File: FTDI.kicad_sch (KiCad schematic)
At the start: 30 parts, among them J301 USB_B_Micro, U301 93LCxxBxxOT, U302 FT2232HQ, Y301 ABM8-12.000MHZ-20

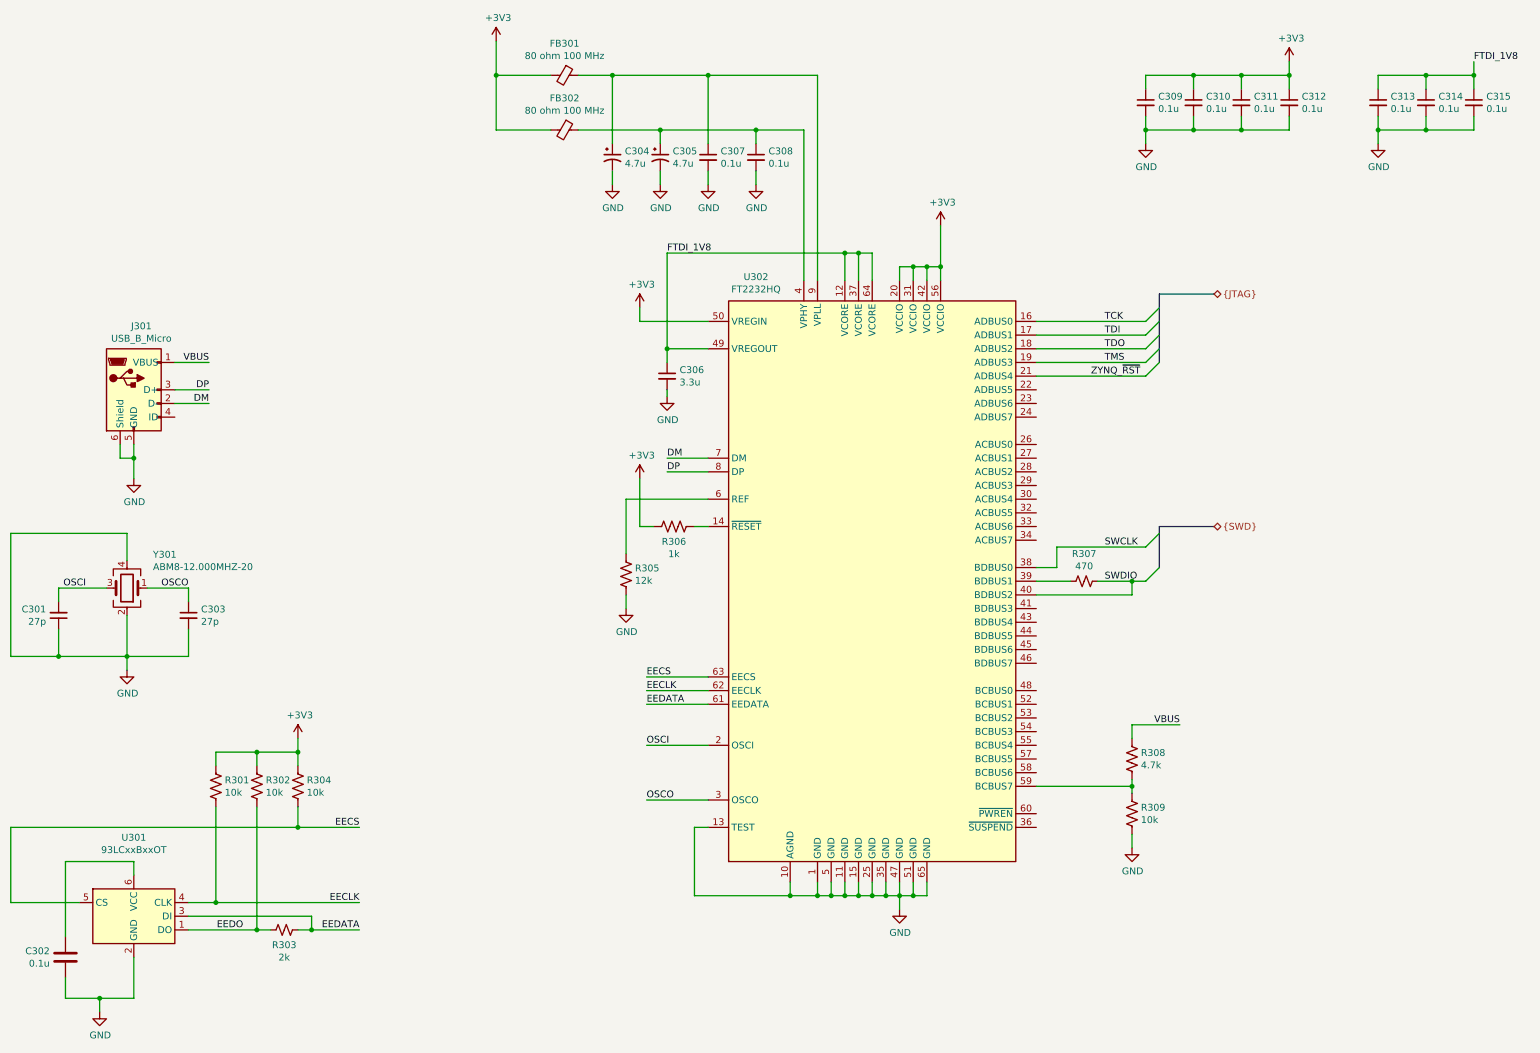
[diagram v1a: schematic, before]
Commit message: Attach ethernet to PL, layout and route
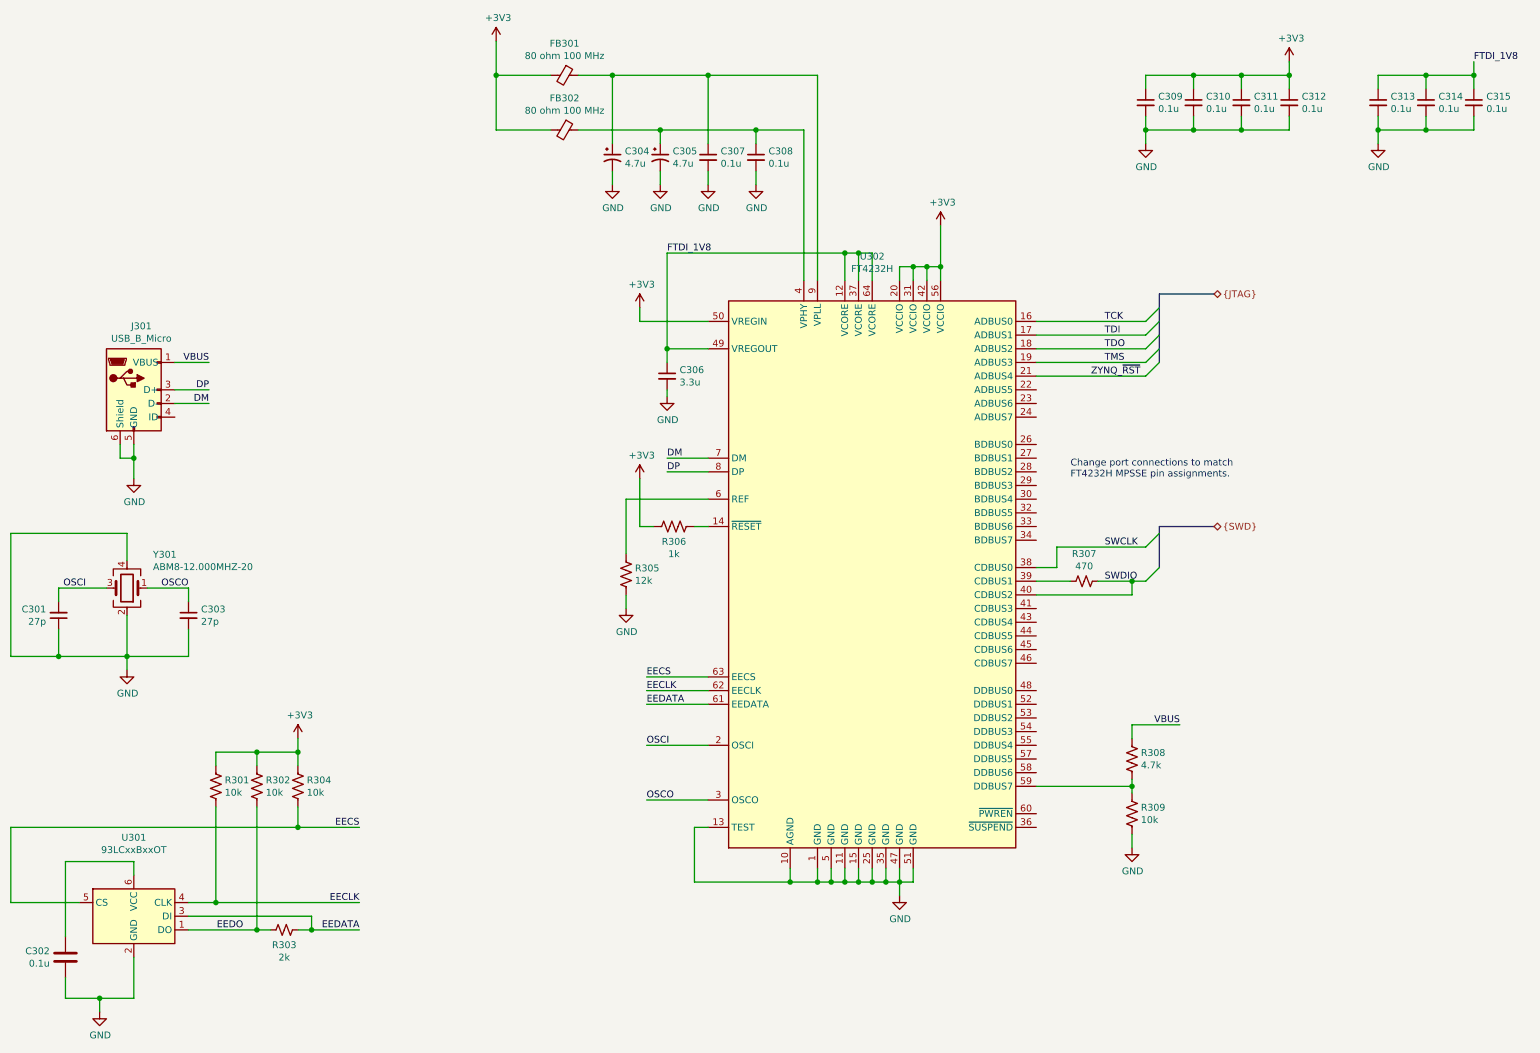
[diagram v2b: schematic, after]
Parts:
- removed U302: FT2232HQ, Package_DFN_QFN:QFN-64-1EP_9x9mm_P0.5mm_EP4.35x4.35mm, symbol Interface_USB:FT2232HQ
- added U302: FT4232H, Package_QFP:LQFP-64_10x10mm_P0.5mm, symbol Interface_USB:FT4232H
- FB301, FB302: footprint Inductor_SMD:L_0603_1608Metric -> Inductor_SMD:L_0402_1005Metric
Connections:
- net +3V3: now also U302.20 (VCCIO), U302.31 (VCCIO), U302.42 (VCCIO), U302.50 (VREGIN), U302.56 (VCCIO)
- net DM: now also U302.7 (DM)
- net DP: now also U302.8 (DP)
- net EECLK: now also U302.62 (EECLK)
- net EECS: now also U302.63 (EECS)
- net EEDATA: now also U302.61 (EEDATA)
- net FTDI_1V8: now also U302.12 (VCORE), U302.37 (VCORE), U302.49 (VREGOUT), U302.64 (VCORE)
- net GND: now also U302.1 (GND), U302.10 (AGND), U302.11 (GND), U302.13 (TEST), U302.15 (GND), U302.25 (GND), U302.35 (GND), U302.47 (GND), U302.5 (GND), U302.51 (GND)
- net OSCI: now also U302.2 (OSCI)
- net OSCO: now also U302.3 (OSCO)
- net SWCLK: now also U302.38 (CDBUS0)
- net SWDIO: now also U302.40 (CDBUS2)
- net TCK: now also U302.16 (ADBUS0)
- net TDI: now also U302.17 (ADBUS1)
- net TDO: now also U302.18 (ADBUS2)
- net TMS: now also U302.19 (ADBUS3)
- net ZYNQ_~RST: now also U302.21 (ADBUS4)
- net at R306.2: now also U302.14 (~RESET)
- net at R308.2, R309.1: now also U302.59 (DDBUS7)
- net at R307.1: now also U302.39 (CDBUS1)
- net at C305.1, C308.1, FB302.1: now also U302.4 (VPHY)
- net at R305.1: now also U302.6 (REF)
- net at C304.1, C307.1, FB301.1: now also U302.9 (VPLL)
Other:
- note added: "Change port connections to match FT4232H MPSSE pin assignments."

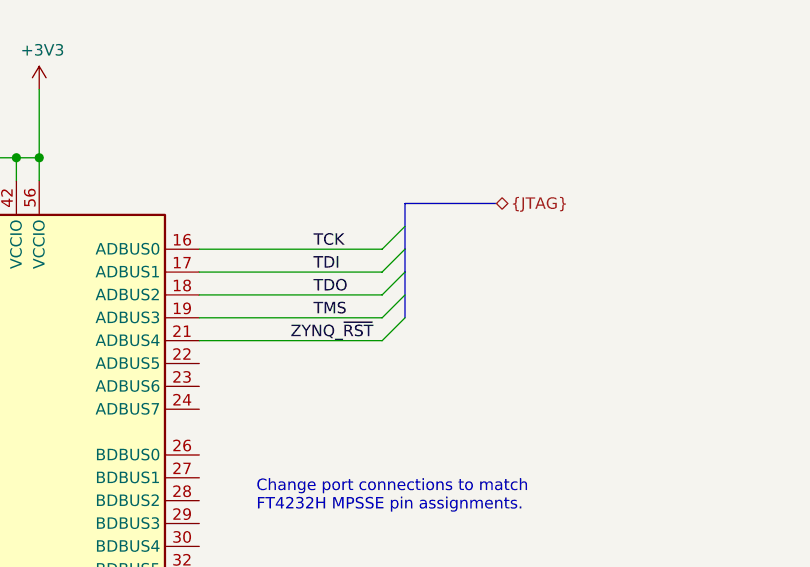
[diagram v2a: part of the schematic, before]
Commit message: Move Ethernet around to save space
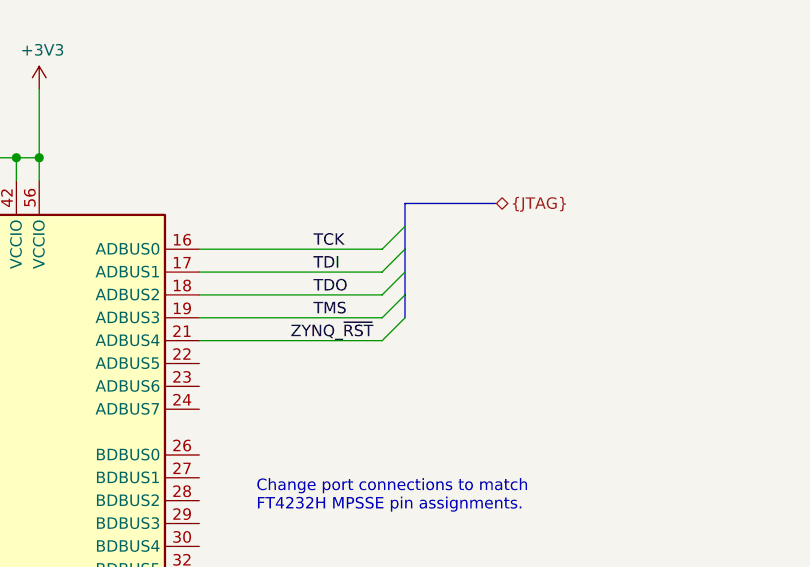
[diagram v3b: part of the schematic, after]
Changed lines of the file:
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@@
-(kicad_sch (version 20200714) (host eeschema "5.99.0-unknown-a146cd9~102~ubuntu20.04.1")
+(kicad_sch (version 20200714) (host eeschema "5.99.0-unknown-9b6ade6b1~102~ubuntu20.04.1")
   (page 3 15)
   (paper "B")
@@
     (stroke (width 0) (type solid) (color 0 0 0 0))
   )
-  (bus (pts (xy 262.89 87.63) (xy 262.89 90.17))
-    (stroke (width 0) (type solid) (color 0 0 0 0))
-  )
-  (bus (pts (xy 262.89 90.17) (xy 262.89 95.25))
-    (stroke (width 0) (type solid) (color 0 0 0 0))
-  )
+  (bus (pts (xy 262.89 87.63) (xy 262.89 92.71))
+    (stroke (width 0) (type solid) (color 0 0 0 0))
+  )
+  (bus (pts (xy 262.89 92.71) (xy 262.89 95.25))
+    (stroke (width 0) (type solid) (color 0 0 0 0))
+  )

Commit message: Expand PCB, change to inches, center Snickerdoodle
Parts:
- removed R308: 4.7k, Resistor_SMD:R_0603_1608Metric, symbol Device:R_US
- removed R309: 10k, Resistor_SMD:R_0603_1608Metric, symbol Device:R_US
- R301, R302, R303, R304, R305, R306, R307: footprint Resistor_SMD:R_0603_1608Metric -> Resistor_SMD:R_0402_1005Metric
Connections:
- net SWCLK: now also U302.26 (BDBUS0); no longer U302.38 (CDBUS0)
- net SWDIO: now also U302.28 (BDBUS2); no longer U302.40 (CDBUS2)
- net ~FTDI_RESET: now reaches R306.2, U302.14 (~RESET)
- net VPLL: now reaches C304.1, C307.1, FB301.1, U302.9 (VPLL)
- net at R307.1: now also U302.27 (BDBUS1); no longer U302.39 (CDBUS1)
- net VPHY: now reaches C305.1, C308.1, FB302.1, U302.4 (VPHY)
- net MCU_~RST: now reaches U302.29 (BDBUS3)
- net REF: now reaches R305.1, U302.6 (REF)
- net DM renamed D-
- net DP renamed D+
- new net FTDI_RX: U302.39 (CDBUS1)
- new net FTDI_TX: U302.38 (CDBUS0)
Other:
- note removed: "Change port connections to match FT4232H MPSSE pin assignments."
- moved on the sheet: R305, R306, R307

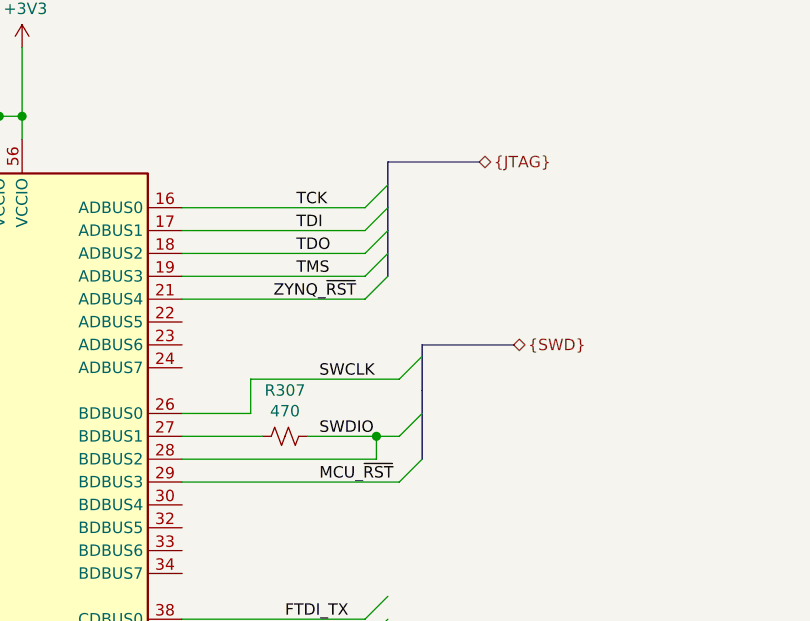
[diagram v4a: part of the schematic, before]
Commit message: Move Ethernet PHY to left side of board
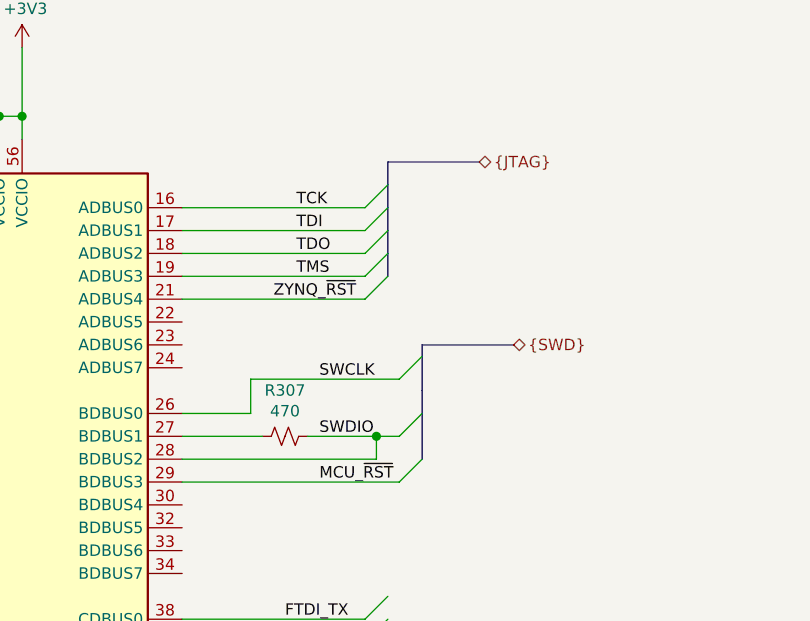
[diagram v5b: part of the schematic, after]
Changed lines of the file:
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@@
-(kicad_sch (version 20200714) (host eeschema "5.99.0-unknown-829316fad~102~ubuntu20.04.1")
+(kicad_sch (version 20200828) (generator eeschema)
   (page 3 15)
   (paper "B")
@@
     (stroke (width 0) (type solid) (color 0 0 0 0))
   )
-  (bus (pts (xy 262.89 82.55) (xy 262.89 87.63))
+  (bus (pts (xy 262.89 82.55) (xy 262.89 85.09))
+    (stroke (width 0) (type solid) (color 0 0 0 0))
+  )
+  (bus (pts (xy 262.89 85.09) (xy 262.89 87.63))
     (stroke (width 0) (type solid) (color 0 0 0 0))
   )
@@
     (stroke (width 0) (type solid) (color 0 0 0 0))
   )
-  (bus (pts (xy 262.89 90.17) (xy 262.89 95.25))
+  (bus (pts (xy 262.89 90.17) (xy 262.89 92.71))
+    (stroke (width 0) (type solid) (color 0 0 0 0))
+  )
+  (bus (pts (xy 262.89 92.71) (xy 262.89 95.25))
     (stroke (width 0) (type solid) (color 0 0 0 0))
   )
@@
     (stroke (width 0.1524) (type solid) (color 0 0 0 0))
   )
-  (bus (pts (xy 266.7 107.95) (xy 266.7 115.57))
-    (stroke (width 0) (type solid) (color 0 0 0 0))
-  )
+  (bus (pts (xy 266.7 107.95) (xy 266.7 110.49))
+    (stroke (width 0) (type solid) (color 0 0 0 0))
+  )
+  (bus (pts (xy 266.7 110.49) (xy 266.7 115.57))
+    (stroke (width 0) (type solid) (color 0 0 0 0))
+  )

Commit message: Layout Ethernet PHY decoupling capacitors
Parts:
- FB301, FB302: value 80 ohm 100 MHz -> 120 ohms; footprint Inductor_SMD:L_0402_1005Metric -> Inductor_SMD:L_0603_1608Metric; LCSC Part Number (none) -> C73100; Manufacturer (none) -> Murata Electronics; Part Number (none) -> BLM18PG121SN1D
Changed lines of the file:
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@@
-(kicad_sch (version 20200828) (generator eeschema)
-  (page 3 15)
+(kicad_sch (version 20201015) (generator eeschema)
+  (page 1 15)
   (paper "B")
   (title_block
@@
     (in_bom yes) (on_board yes)
     (property "Reference" "FB301" (id 0) (at 152.4 35.998 90))
-    (property "Value" "80 ohm 100 MHz" (id 1) (at 152.4 38.2967 90))
-    (property "Footprint" "Inductor_SMD:L_0402_1005Metric" (id 2) (at 152.4 40.132 90)
+    (property "Value" "120 ohms" (id 1) (at 152.4 38.2967 90))
+    (property "Footprint" "Inductor_SMD:L_0603_1608Metric" (id 2) (at 152.4 40.132 90)
       (effects (font (size 1.27 1.27)) hide)
     )
@@
       (effects (font (size 1.27 1.27)) hide)
     )
+    (property "LCSC Part Number" "C73100" (id 4) (at 152.4 41.91 0)
+      (effects (font (size 1.27 1.27)) hide)
+    )
+    (property "Manufacturer" "Murata Electronics" (id 5) (at 152.4 41.91 0)
+      (effects (font (size 1.27 1.27)) hide)
+    )
+    (property "Part Number" "BLM18PG121SN1D" (id 6) (at 152.4 41.91 0)
+      (effects (font (size 1.27 1.27)) hide)
+    )
   )
   (symbol (lib_id "Device:Ferrite_Bead_Small") (at 152.4 52.07 270) (unit 1)
     (in_bom yes) (on_board yes)
     (property "Reference" "FB302" (id 0) (at 152.4 46.158 90))
-    (property "Value" "80 ohm 100 MHz" (id 1) (at 152.4 48.4567 90))
-    (property "Footprint" "Inductor_SMD:L_0402_1005Metric" (id 2) (at 152.4 50.292 90)
+    (property "Value" "120 ohms" (id 1) (at 152.4 48.4567 90))
+    (property "Footprint" "Inductor_SMD:L_0603_1608Metric" (id 2) (at 152.4 50.292 90)
       (effects (font (size 1.27 1.27)) hide)
     )
@@
       (effects (font (size 1.27 1.27)) hide)
     )
+    (property "LCSC Part Number" "C73100" (id 4) (at 152.4 52.07 0)
+      (effects (font (size 1.27 1.27)) hide)
+    )
+    (property "Manufacturer" "Murata Electronics" (id 5) (at 152.4 52.07 0)
+      (effects (font (size 1.27 1.27)) hide)
+    )
+    (property "Part Number" "BLM18PG121SN1D" (id 6) (at 152.4 52.07 0)
+      (effects (font (size 1.27 1.27)) hide)
+    )
